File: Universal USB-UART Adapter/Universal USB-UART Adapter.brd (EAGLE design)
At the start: 22.2 x 15.2 mm, 9 parts, among them U1 FT232RQ, X1 USBPCB

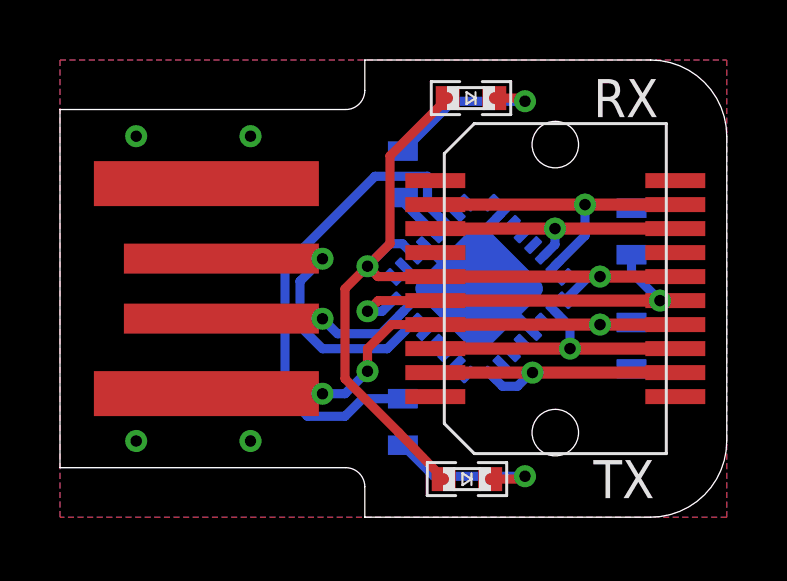
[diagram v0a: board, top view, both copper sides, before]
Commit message: Modified voltage connections to be next to each other. Easier to short.
Signed-off-by: Cruz Monrreal II <Cruz.Monrreal@gmail.com>
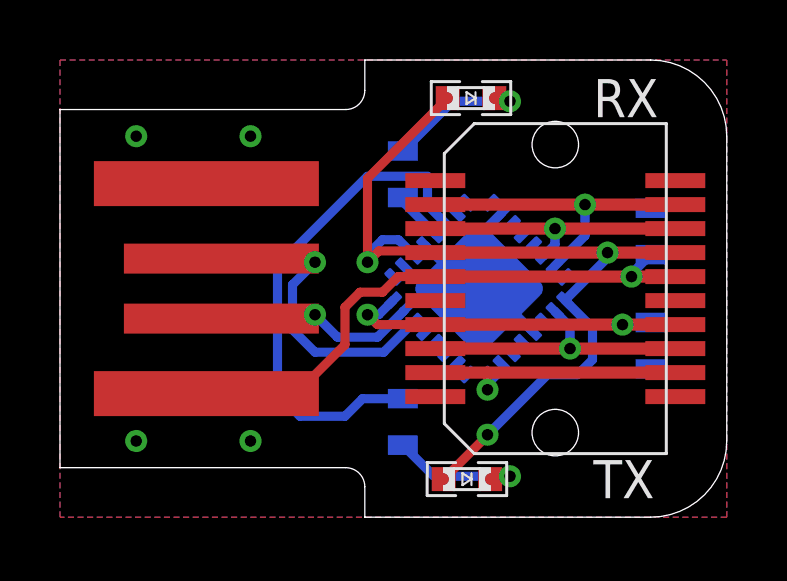
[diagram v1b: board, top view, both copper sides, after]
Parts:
- moved C1 3.86 mm to (19.7, 9.53), turned to 270 degrees
- moved C2 3.86 mm to (19.7, 5.71), turned to 270 degrees
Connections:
- net RX renamed RXI
- net TX renamed TXO
- net 3.3V: now also U$7.4, U$7.4@1; no longer U$7.5, U$7.5@1
- net 5.0V: now also U$7.7, U$7.7@1; no longer U$7.6, U$7.6@1
- net VIN: now also U$7.6, U$7.6@1; no longer U$7.4, U$7.4@1
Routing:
- net 5.0V: track 29.4 -> 30.4 mm, vias 2 -> 3
- net N$3: track 5.70 -> 4.70 mm
- net N$1: track 5.83 -> 4.83 mm
- net 3.3V: track 13.3 -> 12.4 mm
- net VIN: track 18.1 -> 19.0 mm, vias 3 -> 1
- net !CTS: track 9.74 -> 9.12 mm
- net N$2: track 16.6 -> 17.1 mm

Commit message: Changed connector to 2mm pitch as opposed to PCB connector
Signed-off-by: Cruz Monrreal II <Cruz.Monrreal@gmail.com>
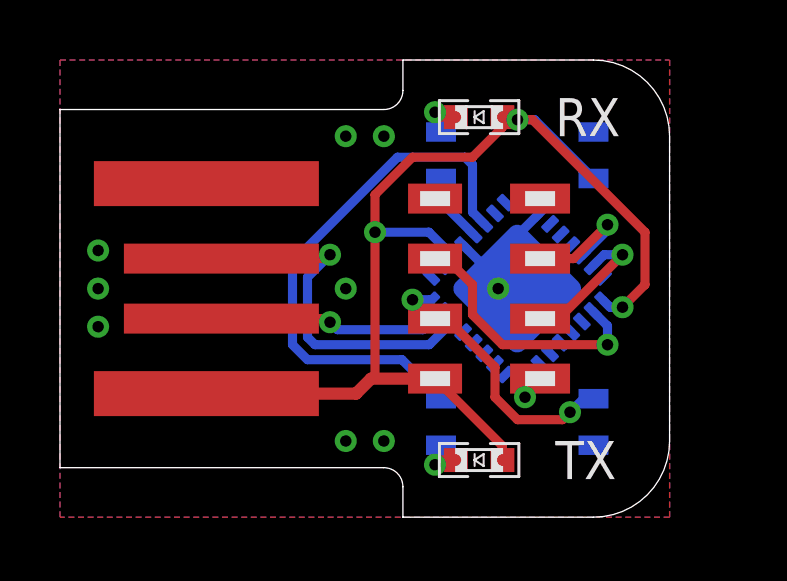
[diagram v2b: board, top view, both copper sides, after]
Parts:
- removed U$7: MEC8-110-02-X-D-RA1, samtec:MEC8-110-02-X-D-RA1
- added U$4: (no value), samtec:MMT-104-01-X-DH-X
- moved C2 3.17 mm to (17.8, 3.17)
- moved C1 3.17 mm to (17.8, 12.1)
- moved R2 1.42 mm to (12.7, 12.1)
- moved R1 1.27 mm to (12.7, 3.17)
- moved U1 1.27 mm to (15.2, 7.62)
- moved TX 0.75 mm to (14.0, 1.91), turned to 180 degrees
- moved RX 0.69 mm to (14.0, 13.3), turned to 180 degrees
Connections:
- removed net VIN: C1.2, U$7.6, U$7.6@1, X1.5V
- net !CTS: now also U$4.8; no longer U$7.2, U$7.2@1
- net !DTR: now also U$4.6; no longer U$7.9, U$7.9@1
- net 3.3V: now also U$4.5; no longer U$7.4, U$7.4@1
- net 5.0V: now also C1.2, U$4.7, X1.5V; no longer U$7.7, U$7.7@1
- net GND: now also U$4.1; no longer U$7.10, U$7.10@1
- net RXI: now also U$4.3; no longer U$7.3, U$7.3@1
- net TXO: now also U$4.4; no longer U$7.8, U$7.8@1
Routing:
- net VIN: track 19.0 -> 0.00 mm, vias 1 -> 0
- net 5.0V: track 30.4 -> 39.3 mm
- net !CTS: track 9.12 -> 1.64 mm
- net !DTR: track 10.5 -> 4.79 mm
- net TXO: track 9.06 -> 4.10 mm
- net N$1: track 4.83 -> 1.51 mm
- net 3.3V: track 12.4 -> 9.20 mm
- net N$3: track 4.70 -> 1.49 mm
- net D+: track 10.5 -> 12.0 mm
- net N$2: track 17.1 -> 18.1 mm
- net D-: track 6.83 -> 7.76 mm
- net N$4: track 1.68 -> 2.32 mm
- net RXI: track 9.47 -> 8.86 mm
- net GND: track 7.59 -> 8.13 mm, vias 4 -> 9
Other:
- board size 22.2 x 15.2 mm -> 20.3 x 15.2 mm
